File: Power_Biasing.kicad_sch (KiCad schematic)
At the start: 17 parts, among them U100 TPS56637RPAR

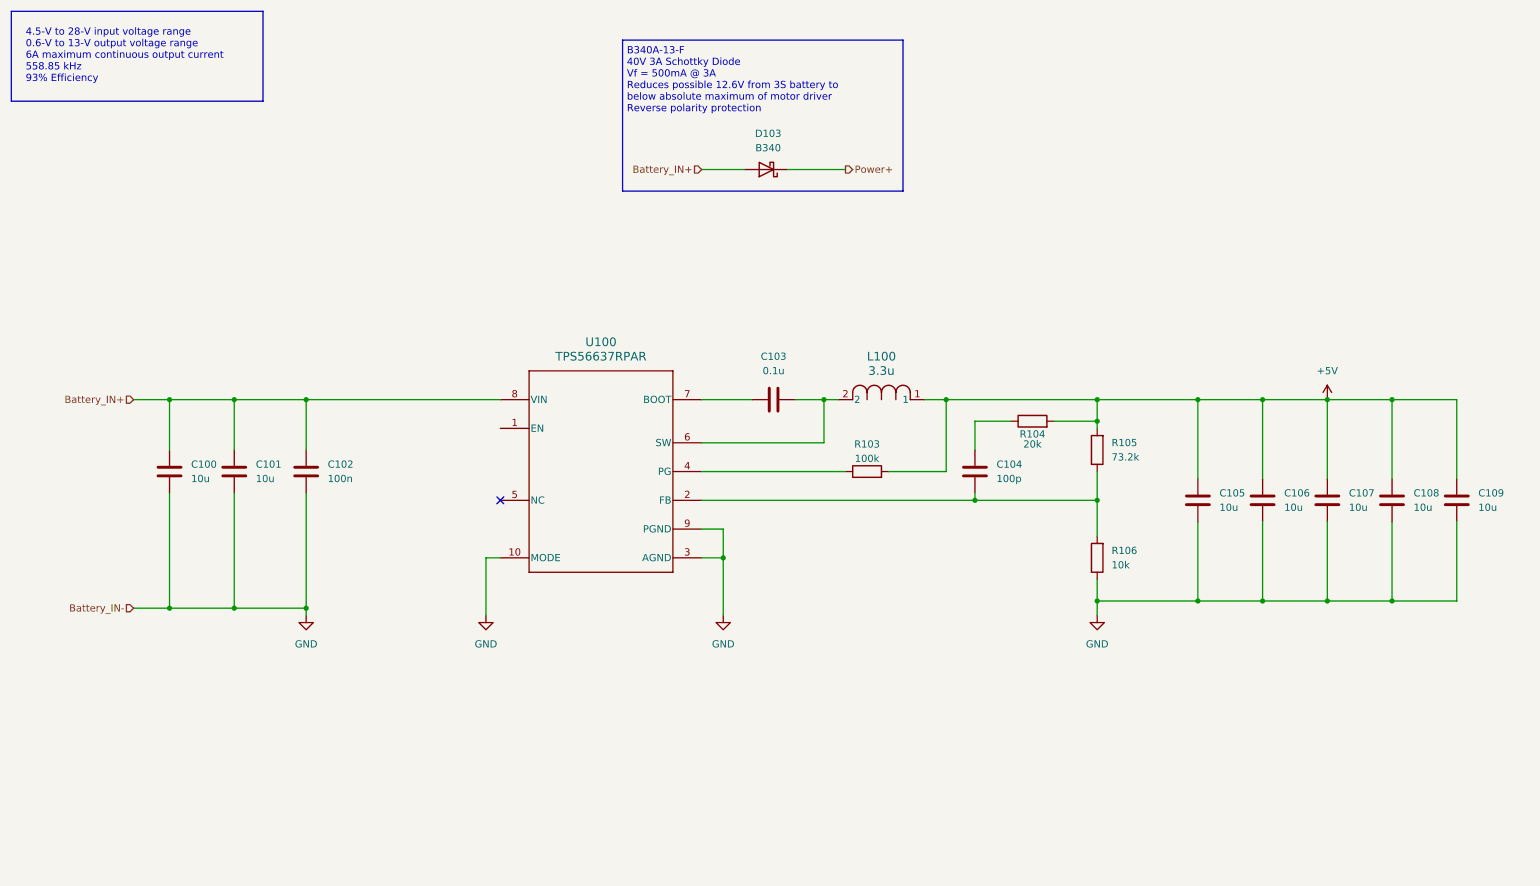
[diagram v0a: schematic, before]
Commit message: Added gyro, current sense, removed servo control, added temp sense
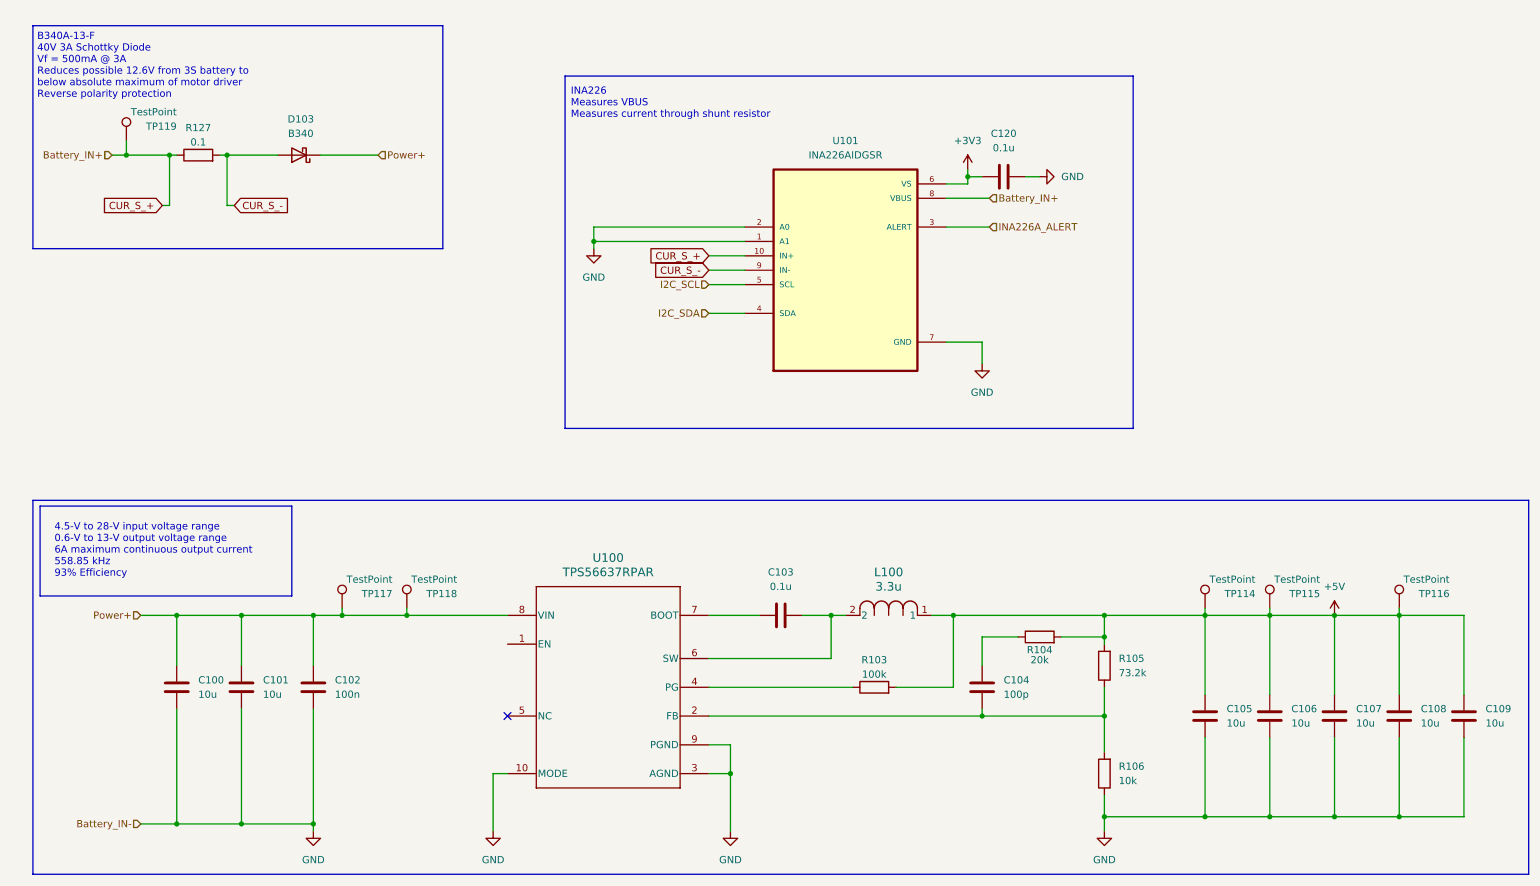
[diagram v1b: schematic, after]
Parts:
- added C120: 0.1u, Capacitor_SMD:C_0805_2012Metric_Pad1.18x1.45mm_HandSolder, symbol Device:C
- added R127: 0.1, Resistor_SMD:R_1210_3225Metric_Pad1.30x2.65mm_HandSolder, symbol Device:R
- added TP114, TP115, TP116, TP117, TP118, TP119: TestPoint, TestPoint:TestPoint_Pad_D2.0mm, symbol Connector:TestPoint
- added U101: INA226AIDGSR, INA226AIDGSR:INA226AIDGSR, symbol INA226AIDGSR:INA226AIDGSR
- U100: footprint RPA0010A -> TPS56637RPAR:RPA0010A
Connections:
- net +5V: now also TP114.1, TP115.1, TP116.1
- net GND: now also C120.2, U101.1 (A1), U101.2 (A0), U101.7 (GND)
- net Power+: now also C100.2, C101.2, C102.2, U100.8 (VIN), TP117.1, TP118.1
- removed net Battery_IN+: C100.2, C101.2, C102.2, D103.2 (A), U100.8 (VIN)
- new net +3V3: C120.1, U101.6 (VS)
- new net CUR_S_+: R127.1, TP119.1, U101.10 (IN+), U101.8 (VBUS)
- new net CUR_S_-: D103.2 (A), R127.2, U101.9 (IN-)
- new net I2C_SCL: U101.5 (SCL)
- new net I2C_SDA: U101.4 (SDA)
- new net INA226A_ALERT: U101.3 (ALERT)
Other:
- note added: "INA226 Measures VBUS Measures current through shunt resistor"
- moved on the sheet: C100, C101, C102, C103, C104, C105, C106, C107, C108, C109, D103, L100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

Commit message: finished up schematic, added magnetic sensor, cleaned up pins, etc.
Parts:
- removed TP114, TP115, TP116, TP117, TP118, TP119: TestPoint, TestPoint:TestPoint_Pad_D2.0mm, symbol Connector:TestPoint
- C100, C101, C105, C106, C107, C108, C109: footprint Capacitor_SMD:C_1206_3216Metric_Pad1.33x1.80mm_HandSolder -> Capacitor_SMD:C_0603_1608Metric_Pad1.08x0.95mm_HandSolder; Digikey https://www.digikey.com/en/products/detail/samsung-electro-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 -> (none)
- C102, C103, C120: footprint Capacitor_SMD:C_0805_2012Metric_Pad1.18x1.45mm_HandSolder -> Capacitor_SMD:C_0603_1608Metric_Pad1.08x0.95mm_HandSolder; Digikey https://www.digikey.com/en/products/detail/murata-electroni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 -> (none)
- C104: footprint Capacitor_SMD:C_0805_2012Metric_Pad1.18x1.45mm_HandSolder -> Capacitor_SMD:C_0603_1608Metric_Pad1.08x0.95mm_HandSolder; Digikey https://www.digikey.com/en/products/detail/kemet/C0805C101K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 -> (none)
- D103: Digikey https://www.digikey.com/en/products/detail/diodes-incorpora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 -> (none)
- L100: Digikey https://www.digikey.com/en/products/detail/vishay-dale/IHLP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 -> (none)
- U100: Digikey https://www.digikey.com/en/products/detail/texas-instrument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 -> (none)

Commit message: added 5V test point at caps
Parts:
- added 5V103: TestPoint, TestPoint:TestPoint_Pad_D1.0mm, symbol Connector:TestPoint
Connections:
- net +5V: now also 5V103.1
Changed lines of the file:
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@@
+	)
+	(symbol
+		(lib_id "Connector:TestPoint")
+		(at 234.95 119.38 0)
+		(unit 1)
+		(exclude_from_sim no)
+		(in_bom yes)
+		(on_board yes)
+		(dnp no)
+		(property "Reference" "5V103"
+			(at 234.95 112.014 90)
+			(effects
+				(font
+					(size 1.27 1.27)
+				)
+				(justify right)
+			)
+		)
+		(property "Value" "TestPoint"
+			(at 243.84 114.3 0)
+			(effects
+				(font
+					(size 1.27 1.27)
+				)
+				(justify right)
+				(hide yes)
+			)
+		)
+		(property "Footprint" "TestPoint:TestPoint_Pad_D1.0mm"
+			(at 240.03 119.38 0)
+			(effects
+				(font
+					(size 1.27 1.27)
+				)
+				(hide yes)
+			)
+		)
+		(property "Datasheet" "~"
+			(at 240.03 119.38 0)
+			(effects
+				(font
+					(size 1.27 1.27)
+				)
+				(hide yes)
+			)
+		)
+		(property "Description" "test point"
+			(at 234.95 119.38 0)
+			(effects
+				(font
+					(size 1.27 1.27)
+				)
+				(hide yes)
+			)
+		)
+		(pin "1"
+		)
+		(instances
+			(project "TeensyDAQ_REV0"
+				(path "/11737956-c422-45b5-a9a0-ee63a853502c/91dc7722-8943-479b-9672-11a66c9c8ce6"
+					(reference "5V103")
+					(unit 1)
+				)
+			)
+		)
 	)
 	(symbol

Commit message: added TVS diodes to external pins for protection. Ran fabrication output. Ran iBOM generation. All part links can be seen in the iBOM. Download and open to see this
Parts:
- C100, C101, C102, C103, C104, C105, C106, C107, C108, C109, C120: DIGIKEY LINK (none) -> https://www.digikey.com/en/products/detail/murata-electroni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
- D103: DIGIKEY LINK (none) -> https://www.digikey.com/en/products/detail/diodes-incorpora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
- L100: DIGIKEY LINK (none) -> https://www.digikey.com/en/products/detail/vishay-dale/IHLP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
- R103, R104, R105, R106: DIGIKEY LINK (none) -> https://www.digikey.com/en/products/detail/yageo/RC0603FR-0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
- R127: DIGIKEY LINK (none) -> https://www.digikey.com/en/products/detail/yageo/RL1210FR-0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
- U100, U101: DIGIKEY LINK (none) -> https://www.digikey.com/en/products/detail/texas-instrument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
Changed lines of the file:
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@@
 	(generator_version "8.0")
 	(paper "A4")
+	(title_block
+		(date "2025-02-11")
+	)
 	(junction
 		(at 246.38 119.38)
@@
 			)
 		)
+		(property "DIGIKEY LINK" "https://www.digikey.com/en/products/detail/texas-instruments/TPS56637RPAR/10715537"
+			(at 118.11 132.08 0)
+			(effects
+				(font
+					(size 1.27 1.27)
+				)
+				(hide yes)
+			)
+		)
 		(pin "10"
 		)
@@
 			)
 		)
+		(property "DIGIKEY LINK" "https://www.digikey.com/en/products/detail/yageo/RC0603FR-07100KL/726889"
+			(at 165.1 132.08 0)
+			(effects
+				(font
+					(size 1.27 1.27)
+				)
+				(hide yes)
+			)
+		)
 		(pin "2"
 		)
@@
 			)
 		)
+		(property "DIGIKEY LINK" "https://www.digikey.com/en/products/detail/murata-electronics/GRM188R61E106KA73D/9867922"
+			(at 234.95 137.16 0)
+			(effects
+				(font
+					(size 1.27 1.27)
+				)
+				(hide yes)
+			)
+		)
 		(pin "2"
 		)
@@
 			)
 		)
+		(property "DIGIKEY LINK" "https://www.digikey.com/en/products/detail/murata-electronics/GRM188R61E106KA73D/9867922"
+			(at 53.34 132.08 0)
+			(effects
+				(font
+					(size 1.27 1.27)
+				)
+				(hide yes)
+			)
+		)
 		(pin "2"
 		)
@@
 			)
 		)
+		(property "DIGIKEY LINK" "https://www.digikey.com/en/products/detail/murata-electronics/GRM188R61E106KA73D/9867922"
+			(at 246.38 137.16 0)
+			(effects
+				(font
+					(size 1.27 1.27)
+				)
+				(hide yes)
+			)
+		)
 		(pin "2"
 		)
@@
 			)
 		)
+		(property "DIGIKEY LINK" "https://www.digikey.com/en/products/detail/murata-electronics/GRM1885C1H101JA01D/586921"
+			(at 184.15 132.08 0)
+			(effects
+				(font
+					(size 1.27 1.27)
+				)
+				(hide yes)
+			)
+		)
 		(pin "2"
 		)
@@
 			)
 		)
+		(property "DIGIKEY LINK" "https://www.digikey.com/en/products/detail/murata-electronics/GRM188R61E106KA73D/9867922"
+			(at 257.81 137.16 0)
+			(effects
+				(font
+					(size 1.27 1.27)
+				)
+				(hide yes)
+			)
+		)
 		(pin "2"
 		)
@@
 			)
 		)
+		(property "DIGIKEY LINK" "https://www.digikey.com/en/products/detail/murata-electronics/GCJ188R71E104KA12D/7363221"
+			(at 66.04 132.08 0)
+			(effects
+				(font
+					(size 1.27 1.27)
+				)
+				(hide yes)
+			)
+		)
 		(pin "2"
 		)
@@
 			)
 		)
+		(property "DIGIKEY LINK" "https://www.digikey.com/en/products/detail/murata-electronics/GRM188R61E106KA73D/9867922"
+			(at 269.24 137.16 0)
+			(effects
+				(font
+					(size 1.27 1.27)
+				)
+				(hide yes)
+			)
+		)
 		(pin "2"
 		)
@@
 			)
 		)
+		(property "DIGIKEY LINK" "https://www.digikey.com/en/products/detail/murata-electronics/GCJ188R71E104KA12D/7363221"
+			(at 187.96 41.91 0)
+			(effects
+				(font
+					(size 1.27 1.27)
+				)
+				(hide yes)
+			)
+		)
 		(pin "2"
 		)
@@
 			)
 		)
+		(property "DIGIKEY LINK" "https://www.digikey.com/en/products/detail/diodes-incorporated/B340-13-F/768768"
+			(at 63.5 38.1 0)
+			(effects
+				(font
+					(size 1.27 1.27)
+				)
+				(hide yes)
+			)
+		)
 		(pin "1"
 		)
@@
 			)
 		)
+		(property "DIGIKEY LINK" "https://www.digikey.com/en/products/detail/texas-instruments/INA226AIDGSR/2687236"
+			(at 160.02 58.42 0)
+			(effects
+				(font
+					(size 1.27 1.27)
+				)
+				(hide yes)
+			)
+		)
 		(pin "7"
 		)
@@
 			)
 		)
+		(property "DIGIKEY LINK" "https://www.digikey.com/en/products/detail/yageo/RL1210FR-070R1L/2827679"
+			(at 45.72 38.1 0)
+			(effects
+				(font
+					(size 1.27 1.27)
+				)
+				(hide yes)
+			)
+		)
 		(pin "2"
 		)
@@
 			)
 		)
+		(property "DIGIKEY LINK" "https://www.digikey.com/en/products/detail/murata-electronics/GRM188R61E106KA73D/9867922"
+			(at 41.91 132.08 0)
+			(effects
+				(font
+					(size 1.27 1.27)
+				)
+				(hide yes)
+			)
+		)
 		(pin "2"
 		)
@@
 			)
 		)
+		(property "DIGIKEY LINK" "https://www.digikey.com/en/products/detail/vishay-dale/IHLP4040DZER3R3M01/1220693"
+			(at 160.02 119.38 0)
+			(effects
+				(font
+					(size 1.27 1.27)
+				)
+				(hide yes)
+			)
+		)
 		(pin "2"
 		)
@@
 			)
 		)
+		(property "DIGIKEY LINK" "https://www.digikey.com/en/products/detail/yageo/RC0603FR-0773K2L/727374"
+			(at 205.74 128.27 0)
+			(effects
+				(font
+					(size 1.27 1.27)
+				)
+				(hide yes)
+			)
+		)
 		(pin "2"
 		)
@@
 			)
 		)
+		(property "DIGIKEY LINK" "https://www.digikey.com/en/products/detail/murata-electronics/GCJ188R71E104KA12D/7363221"
+			(at 148.59 119.38 0)
+			(effects
+				(font
+					(size 1.27 1.27)
+				)
+				(hide yes)
+			)
+		)
 		(pin "2"
 		)
@@
 			)
 		)
+		(property "DIGIKEY LINK" "https://www.digikey.com/en/products/detail/yageo/RC0603FR-0710KL/726880"
+			(at 205.74 147.32 0)
+			(effects
+				(font
+					(size 1.27 1.27)
+				)
+				(hide yes)
+			)
+		)
 		(pin "2"
 		)
@@
 			)
 		)
+		(property "DIGIKEY LINK" "https://www.digikey.com/en/products/detail/yageo/RC0603FR-0720KL/727040"
+			(at 194.31 123.19 0)
+			(effects
+				(font
+					(size 1.27 1.27)
+				)
+				(hide yes)
+			)
+		)
 		(pin "2"
 		)
@@
 			(at 223.52 137.16 0)
 			(effects
+				(font
+					(size 1.27 1.27)
+				)
+				(hide yes)
+			)
+		)
+		(property "DIGIKEY LINK" "https://www.digikey.com/en/products/detail/murata-electronics/GRM188R61E106KA73D/9867922"
+			(at 223.52 137.16 0)
+			(effects

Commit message: added power planes to correct layer. Added 10A 1206 fuse to battery input before current measurement resistor and reverse polarity diode
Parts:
- added F100: Fuse, Fuse:Fuse_1206_3216Metric, symbol Device:Fuse
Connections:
- net CUR_S_+: now also F100.2
- new net Battery_IN+: F100.1
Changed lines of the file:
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@@
+	(wire
+		(pts
+			(xy 39.37 38.1) (xy 40.64 38.1)
+		)
+		(stroke
+			(width 0)
+			(type default)
+		)
+	)
 	(wire
 		(pts
@@
 	(wire
 		(pts
-			(xy 30.48 38.1) (xy 40.64 38.1)
+			(xy 30.48 38.1) (xy 31.75 38.1)
 		)
 		(stroke
@@
 			)
 			(justify left)
+		)
+	)
+	(global_label "CUR_S_+"
+		(shape input)
+		(at 185.42 45.72 0)
+		(fields_autoplaced yes)
+		(effects
+			(font
+				(size 1.27 1.27)
+			)
+			(justify left)
+		)
+		(property "Intersheetrefs" "${INTERSHEET_REFS}"
+			(at 196.9928 45.72 0)
+			(effects
+				(font
+					(size 1.27 1.27)
+				)
+				(justify left)
+				(hide yes)
+			)
 		)
 	)
@@
 	(hierarchical_label "Battery_IN+"
 		(shape input)
-		(at 185.42 45.72 0)
-		(effects
-			(font
-				(size 1.27 1.27)
-			)
-			(justify left)
-		)
-	)
-	(hierarchical_label "Battery_IN+"
-		(shape input)
 		(at 30.48 38.1 180)
 		(effects
@@
 					(unit 1)
 				)
+			)
+		)
+	)
+	(symbol
+		(lib_id "Device:Fuse")
+		(at 35.56 38.1 90)
+		(unit 1)
+		(exclude_from_sim no)
+		(in_bom yes)
+		(on_board yes)
+		(dnp no)
+		(fields_autoplaced yes)
+		(property "Reference" "F100"
+			(at 35.56 31.75 90)
+			(effects
+				(font
+					(size 1.27 1.27)
+				)
+			)
+		)
+		(property "Value" "Fuse"
+			(at 35.56 34.29 90)
+			(effects
+				(font
+					(size 1.27 1.27)
+				)
+			)
+		)
+		(property "Footprint" "Fuse:Fuse_1206_3216Metric"
+			(at 35.56 39.878 90)
+			(effects
+				(font
+					(size 1.27 1.27)
+				)
+				(hide yes)
+			)
+		)
+		(property "Datasheet" "~"
+			(at 35.56 38.1 0)
+			(effects
+				(font
+					(size 1.27 1.27)
+				)
+				(hide yes)
+			)
+		)
+		(property "Description" "Fuse"
+			(at 35.56 38.1 0)
+			(effects
+				(font
+					(size 1.27 1.27)
+				)
+				(hide yes)
+			)
+		)
+		(property "DIGIKEY LINK" "https://www.digikey.com/en/products/detail/bel-fuse-inc/0685H9100-01/5466705"
+			(at 35.56 38.1 90)
+			(effects
+				(font
+					(size 1.27 1.27)
+				)
+				(hide yes)
+			)
+		)
+		(pin "2"
+		)
+		(pin "1"
+		)
+		(instances
+			(project ""
+				(path "/11737956-c422-45b5-a9a0-ee63a853502c/91dc7722-8943-479b-9672-11a66c9c8ce6"
+					(reference "F100")
+					(unit 1)
+				)
